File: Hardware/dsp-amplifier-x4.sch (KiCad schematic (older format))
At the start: 64 parts, among them J1 USBi, J2 EXT, J3 Raspberry_Pi_2_3, J4 Screw_Terminal_01x02, J5 Screw_Terminal_01x02, J6 Screw_Terminal_01x02, J7 Screw_Terminal_01x02, P1 Conn_WallPlug, Q1 STD2805, U1 ADAU1452

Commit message: new sockets
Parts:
- J4, J5, J6, J7, P1: footprint TerminalBlock:TerminalBlock_Wuerth_691311400102_P7.62mm -> terminal_connectors:wuerth_691216410002
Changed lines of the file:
@@
 F 0 "J4" H 14780 2792 50  0000 L CNN
 F 1 "Screw_Terminal_01x02" H 14780 2701 50  0000 L CNN
-F 2 "TerminalBlock:TerminalBlock_Wuerth_691311400102_P7.62mm" H 14700 2800 50  0001 C CNN
+F 2 "terminal_connectors:wuerth_691216410002" H 14700 2800 50  0001 C CNN
 F 3 "~" H 14700 2800 50  0001 C CNN
 	1    14700 2800
@@
 F 0 "J5" H 14780 3142 50  0000 L CNN
 F 1 "Screw_Terminal_01x02" H 14780 3051 50  0000 L CNN
-F 2 "TerminalBlock:TerminalBlock_Wuerth_691311400102_P7.62mm" H 14700 3150 50  0001 C CNN
+F 2 "terminal_connectors:wuerth_691216410002" H 14700 3150 50  0001 C CNN
 F 3 "~" H 14700 3150 50  0001 C CNN
 	1    14700 3150
@@
 F 0 "J6" H 14780 4492 50  0000 L CNN
 F 1 "Screw_Terminal_01x02" H 14780 4401 50  0000 L CNN
-F 2 "TerminalBlock:TerminalBlock_Wuerth_691311400102_P7.62mm" H 14700 4500 50  0001 C CNN
+F 2 "terminal_connectors:wuerth_691216410002" H 14700 4500 50  0001 C CNN
 F 3 "~" H 14700 4500 50  0001 C CNN
 	1    14700 4500
@@
 F 0 "J7" H 14780 4842 50  0000 L CNN
 F 1 "Screw_Terminal_01x02" H 14780 4751 50  0000 L CNN
-F 2 "TerminalBlock:TerminalBlock_Wuerth_691311400102_P7.62mm" H 14700 4850 50  0001 C CNN
+F 2 "terminal_connectors:wuerth_691216410002" H 14700 4850 50  0001 C CNN
 F 3 "~" H 14700 4850 50  0001 C CNN
 	1    14700 4850
@@
 F 0 "P1" H 9067 1375 50  0000 C CNN
 F 1 "Conn_WallPlug" H 9067 1284 50  0000 C CNN
-F 2 "TerminalBlock:TerminalBlock_Wuerth_691311400102_P7.62mm" H 9450 1050 50  0001 C CNN
+F 2 "terminal_connectors:wuerth_691216410002" H 9450 1050 50  0001 C CNN
 F 3 "~" H 9450 1050 50  0001 C CNN
 	1    9050 1050

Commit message: production v0.1 with gerber
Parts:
- added TP1: TestPoint, TestPoint:TestPoint_Pad_D1.0mm, symbol Connector:TestPoint
- added TP2: NCS, TestPoint:TestPoint_Pad_D1.0mm, symbol Connector:TestPoint
- added TP3: MISO, TestPoint:TestPoint_Pad_D1.0mm, symbol Connector:TestPoint
- added TP4: MOSI, TestPoint:TestPoint_Pad_D1.0mm, symbol Connector:TestPoint
- added TP5: SCLK, TestPoint:TestPoint_Pad_D1.0mm, symbol Connector:TestPoint
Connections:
- net +3.3VA: no longer Q1.3 (E), R4.1
- net +3V3: now also Q1.3 (E), R4.1
- net PI_MISO0: now also TP3.1
- net PI_MOSI0: now also TP4.1
- net PI_NCE0: now also TP2.1
- net PI_SCLK0: now also TP5.1
- net at U1.23 (CLKOUT): now also TP1.1
- no-connect marks 33 -> 35
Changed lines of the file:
@@
 F9 "CLK7" O R 10500 2450 60
 $EndSheet
-$Comp
-L DSP_AnalogDevices:ADAU1452 U1
-U 1 1 6065B65B
-P 3500 3650
-F 0 "U1" H 3500 5731 50  0000 C CNN
-F 1 "ADAU1452" H 3500 5640 50  0000 C CNN
-F 2 "Package_CSP:LFCSP-72-1EP_10x10mm_P0.5mm_EP5.3x5.3mm" H 3500 3650 50  0001 C CNN
-F 3 "https://www.analog.com/media/en/technical-documentation/data-sheets/ADAU1452_1451_1450.pdf" H 3500 3650 50  0001 C CNN
-	1    3500 3650
-	1    0    0    -1
-$EndComp
 Text Label 2000 2350 0    60   ~ 0
 DSP_CLOCK
@@
 Text Label 10850 7950 0    60   ~ 0
 PI_MISO0
-Wire Wire Line
-	10650 7950 11250 7950
-Wire Wire Line
-	11250 8050 10650 8050
 Text Label 10850 8150 0    60   ~ 0
 PI_SCLK0
-Wire Wire Line
-	11250 8150 10650 8150
 Text Label 8350 8350 0    60   ~ 0
 PI_MUTE
@@
 	1700 1450 2000 1450
 Connection ~ 2000 1450
-Text Label 4050 7050 2    60   ~ 0
-PVDD
 Text Label 3300 1250 3    60   ~ 0
 PVDD
@@
 Text Label 3700 9800 3    60   ~ 0
 AVDD
-NoConn ~ 4400 2350
 Text Label 4900 1950 2    60   ~ 0
 VDRIVE
@@
 	0    1    1    0
 $EndComp
-Wire Wire Line
-	4400 3350 4450 3350
 Wire Wire Line
 	4450 3450 4400 3450
@@
 Wire Wire Line
 	2000 4150 2600 4150
+Text Label 4050 7050 2    60   ~ 0
+IOVDD
+$Comp
+L Connector:TestPoint TP1
+U 1 1 6072217C
+P 4450 2350
+F 0 "TP1" V 4404 2538 50  0000 L CNN
+F 1 "TestPoint" V 4495 2538 50  0000 L CNN
+F 2 "TestPoint:TestPoint_Pad_D1.0mm" H 4650 2350 50  0001 C CNN
+F 3 "~" H 4650 2350 50  0001 C CNN
+	1    4450 2350
+	0    1    1    0
+$EndComp
+$Comp
+L DSP_AnalogDevices:ADAU1452 U1
+U 1 1 6065B65B
+P 3500 3650
+F 0 "U1" H 3500 5731 50  0000 C CNN
+F 1 "ADAU1452" H 3500 5640 50  0000 C CNN
+F 2 "Package_CSP:LFCSP-72-1EP_10x10mm_P0.5mm_EP5.3x5.3mm" H 3500 3650 50  0001 C CNN
+F 3 "https://www.analog.com/media/en/technical-documentation/data-sheets/ADAU1452_1451_1450.pdf" H 3500 3650 50  0001 C CNN
+	1    3500 3650
+	1    0    0    -1
+$EndComp
+Wire Wire Line
+	4450 2350 4400 2350
+NoConn ~ 4400 3350
+NoConn ~ 2600 4050
+NoConn ~ 2600 4250
+$Comp
+L Connector:TestPoint TP3
+U 1 1 607AA7B9
+P 11700 7950
+F 0 "TP3" V 11654 8138 50  0000 L CNN
+F 1 "MISO" V 11745 8138 50  0000 L CNN
+F 2 "TestPoint:TestPoint_Pad_D1.0mm" H 11900 7950 50  0001 C CNN
+F 3 "~" H 11900 7950 50  0001 C CNN
+	1    11700 7950
+	0    1    1    0
+$EndComp
+$Comp
+L Connector:TestPoint TP4
+U 1 1 607C870C
+P 12150 8050
+F 0 "TP4" V 12104 8238 50  0000 L CNN
+F 1 "MOSI" V 12195 8238 50  0000 L CNN
+F 2 "TestPoint:TestPoint_Pad_D1.0mm" H 12350 8050 50  0001 C CNN
+F 3 "~" H 12350 8050 50  0001 C CNN
+	1    12150 8050
+	0    1    1    0
+$EndComp
+$Comp
+L Connector:TestPoint TP5
+U 1 1 607E5FAD
+P 12600 8150
+F 0 "TP5" V 12554 8338 50  0000 L CNN
+F 1 "SCLK" V 12645 8338 50  0000 L CNN
+F 2 "TestPoint:TestPoint_Pad_D1.0mm" H 12800 8150 50  0001 C CNN
+F 3 "~" H 12800 8150 50  0001 C CNN
+	1    12600 8150
+	0    1    1    0
+$EndComp
+$Comp
+L Connector:TestPoint TP2
+U 1 1 6082322F
+P 11250 7850
+F 0 "TP2" V 11204 8038 50  0000 L CNN
+F 1 "NCS" V 11295 8038 50  0000 L CNN
+F 2 "TestPoint:TestPoint_Pad_D1.0mm" H 11450 7850 50  0001 C CNN
+F 3 "~" H 11450 7850 50  0001 C CNN
+	1    11250 7850
+	0    1    1    0
+$EndComp
+Wire Wire Line
+	10650 7950 11700 7950
+Wire Wire Line
+	10650 8050 12150 8050
+Wire Wire Line
+	10650 8150 12600 8150
 $EndSCHEMATC

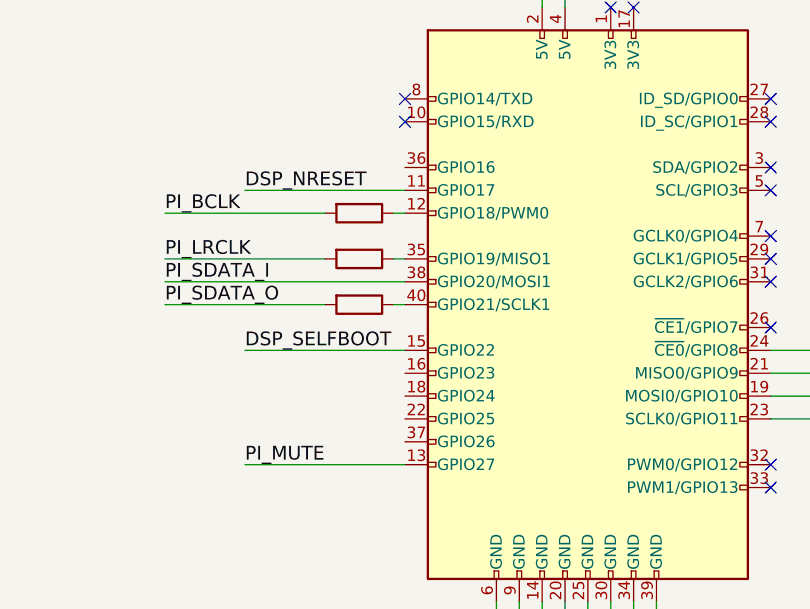
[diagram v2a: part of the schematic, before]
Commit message: fixed usbi/ext header positions
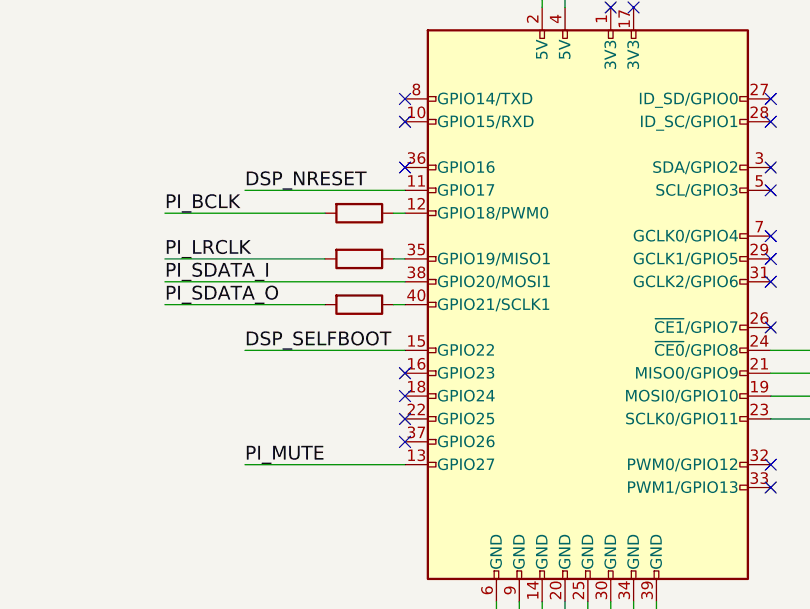
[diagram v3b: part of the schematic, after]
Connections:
- no-connect marks 35 -> 40
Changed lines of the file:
@@
 Wire Wire Line
 	10650 8150 12600 8150
+NoConn ~ 9050 7050
+NoConn ~ 9050 7950
+NoConn ~ 9050 8050
+NoConn ~ 9050 8150
+NoConn ~ 9050 8250
 $EndSCHEMATC

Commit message: hardware bugfixes
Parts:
- added U2: TSOP583xx, OptoDevice:Vishay_MINICAST-3Pin, symbol Interface_Optical:TSOP583xx
- RV1, RV2: footprint Potentiometer_THT:Potentiometer_Vishay_248GJ-249GJ_Single_Vertical -> Potentiometer_THT:Potentiometer_Bourns_PTV09A-1_Single_Vertical
- renumbered R20 to R15, R22 to R16, R23 to R17, R24 to R18, R25 to R19, R26 to R20, R27 to R21, R28 to R22, R29 to R23, R30 to R24
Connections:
- net +24V: no longer J2.1 (Pin_1)
- net +5VA: now also J2.1 (Pin_1)
- net GND: now also U2.2 (GND)
- net PI_3V3: now reaches J3.1 (3V3)
- net PI_3V3: now also U2.3 (Vs)
- net IR_INPUT: now reaches J3.3 (SDA/GPIO2)
- net IR_INPUT: now also U2.1 (OUT)
- no-connect marks 40 -> 38

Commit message: various bugfixes
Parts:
- removed TP1: TestPoint, TestPoint:TestPoint_Pad_D1.0mm, symbol Connector:TestPoint
- removed TP2: NCS, TestPoint:TestPoint_Pad_D1.0mm, symbol Connector:TestPoint
- removed TP3: MISO, TestPoint:TestPoint_Pad_D1.0mm, symbol Connector:TestPoint
- removed TP4: MOSI, TestPoint:TestPoint_Pad_D1.0mm, symbol Connector:TestPoint
- removed TP5: SCLK, TestPoint:TestPoint_Pad_D1.0mm, symbol Connector:TestPoint
- FB1: value 600/100M -> BLM18SP601SZ1D (600/100M)
- RV1, RV2: value R_POT -> PTV09A-1020F-B203
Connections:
- no-connect marks 38 -> 39
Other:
- moved on the sheet: RV1, RV2
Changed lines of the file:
@@
 Wire Wire Line
 	9650 6300 9650 6350
-Text Label 10850 7850 0    60   ~ 0
+Text Label 11250 7850 2    60   ~ 0
 PI_NCE0
 Wire Wire Line
 	11250 7850 10650 7850
-Text Label 10850 8050 0    60   ~ 0
+Text Label 11250 8050 2    60   ~ 0
 PI_MOSI0
-Text Label 10850 7950 0    60   ~ 0
+Text Label 11250 7950 2    60   ~ 0
 PI_MISO0
-Text Label 10850 8150 0    60   ~ 0
+Text Label 11250 8150 2    60   ~ 0
 PI_SCLK0
 Text Label 8350 8350 0    60   ~ 0
@@
 AR Path="/612BC3BD" Ref="FB1"  Part="1"
 F 0 "FB1" V 1326 6850 50  0000 C CNN
-F 1 "600/100M" V 1417 6850 50  0000 C CNN
+F 1 "BLM18SP601SZ1D (600/100M)" V 1417 6850 50  0000 C CNN
 F 2 "Inductor_SMD:L_0603_1608Metric_Pad1.05x0.95mm_HandSolder" V 1530 6850 50  0001 C CNN
 F 3 "~" H 1600 6850 50  0001 C CNN
@@
 L Device:R_POT RV1
 U 1 1 607C4CE2
-P 5850 2100
-F 0 "RV1" H 5781 2146 50  0000 R CNN
-F 1 "R_POT" H 5781 2055 50  0000 R CNN
-F 2 "Potentiometer_THT:Potentiometer_Bourns_PTV09A-1_Single_Vertical" H 5850 2100 50  0001 C CNN
-F 3 "~" H 5850 2100 50  0001 C CNN
-	1    5850 2100
+P 4950 1250
+F 0 "RV1" H 4881 1296 50  0000 R CNN
+F 1 "PTV09A-1020F-B203" H 4881 1205 50  0000 R CNN
+F 2 "Potentiometer_THT:Potentiometer_Bourns_PTV09A-1_Single_Vertical" H 4950 1250 50  0001 C CNN
+F 3 "~" H 4950 1250 50  0001 C CNN
+	1    4950 1250
 	1    0    0    -1
 $EndComp
@@
 L Device:R_POT RV2
 U 1 1 607C7CF2
-P 6850 2100
-F 0 "RV2" H 6781 2146 50  0000 R CNN
-F 1 "R_POT" H 6781 2055 50  0000 R CNN
-F 2 "Potentiometer_THT:Potentiometer_Bourns_PTV09A-1_Single_Vertical" H 6850 2100 50  0001 C CNN
-F 3 "~" H 6850 2100 50  0001 C CNN
-	1    6850 2100
-	1    0    0    -1
-$EndComp
-Text Label 5850 1650 3    60   ~ 0
-AVDD
-Wire Wire Line
-	5850 1650 5850 1900
-Wire Wire Line
-	5850 1900 6850 1900
-Wire Wire Line
-	6850 1900 6850 1950
-Connection ~ 5850 1900
-Wire Wire Line
-	5850 1900 5850 1950
-$Comp
-L power:GND #PWR021
-U 1 1 607F06EF
-P 5850 2300
-F 0 "#PWR021" H 5850 2050 50  0001 C CNN
-F 1 "GND" H 5850 2150 50  0000 C CNN
-F 2 "" H 5850 2300 50  0001 C CNN
-F 3 "" H 5850 2300 50  0001 C CNN
-	1    5850 2300
-	1    0    0    -1
-$EndComp
-Wire Wire Line
-	5850 2250 5850 2300
-$Comp
-L power:GND #PWR023
-U 1 1 608051CA
-P 6850 2300
-F 0 "#PWR023" H 6850 2050 50  0001 C CNN
-F 1 "GND" H 6850 2150 50  0000 C CNN
-F 2 "" H 6850 2300 50  0001 C CNN
-F 3 "" H 6850 2300 50  0001 C CNN
-	1    6850 2300
-	1    0    0    -1
-$EndComp
-Wire Wire Line
-	6850 2300 6850 2250
-Text Label 6350 2100 2    60   ~ 0
+P 5950 1250
+F 0 "RV2" H 5881 1296 50  0000 R CNN
+F 1 "PTV09A-1020F-B203" H 5881 1205 50  0000 R CNN
+F 2 "Potentiometer_THT:Potentiometer_Bourns_PTV09A-1_Single_Vertical" H 5950 1250 50  0001 C CNN
+F 3 "~" H 5950 1250 50  0001 C CNN
+	1    5950 1250
+	1    0    0    -1
+$EndComp
+Wire Wire Line
+	4950 800  4950 1050
+Wire Wire Line
+	4950 1050 5950 1050
+Wire Wire Line
+	5950 1050 5950 1100
+Connection ~ 4950 1050
+Wire Wire Line
+	4950 1050 4950 1100
+Text Label 5450 1250 2    60   ~ 0
 VPOT0
 Wire Wire Line
-	6000 2100 6350 2100
-Text Label 7350 2100 2    60   ~ 0
+	5100 1250 5450 1250
+Text Label 6450 1250 2    60   ~ 0
 VPOT1
 Wire Wire Line
-	7000 2100 7350 2100
+	6100 1250 6450 1250
 Text Label 2250 4750 0    60   ~ 0
 VPOT0
@@
 IOVDD
 $Comp
-L Connector:TestPoint TP1
-U 1 1 6072217C
-P 4450 2350
-F 0 "TP1" V 4404 2538 50  0000 L CNN
-F 1 "TestPoint" V 4495 2538 50  0000 L CNN
-F 2 "TestPoint:TestPoint_Pad_D1.0mm" H 4650 2350 50  0001 C CNN
-F 3 "~" H 4650 2350 50  0001 C CNN
-	1    4450 2350
-	0    1    1    0
-$EndComp
-$Comp
 L DSP_AnalogDevices:ADAU1452 U1
 U 1 1 6065B65B
@@
 	1    0    0    -1
 $EndComp
-Wire Wire Line
-	4450 2350 4400 2350
 NoConn ~ 4400 3350
 NoConn ~ 2600 4050
 NoConn ~ 2600 4250
-$Comp
-L Connector:TestPoint TP3
-U 1 1 607AA7B9
-P 11700 7950
-F 0 "TP3" V 11654 8138 50  0000 L CNN
-F 1 "MISO" V 11745 8138 50  0000 L CNN
-F 2 "TestPoint:TestPoint_Pad_D1.0mm" H 11900 7950 50  0001 C CNN
-F 3 "~" H 11900 7950 50  0001 C CNN
-	1    11700 7950
-	0    1    1    0
-$EndComp
-$Comp
-L Connector:TestPoint TP4
-U 1 1 607C870C
-P 12150 8050
-F 0 "TP4" V 12104 8238 50  0000 L CNN
-F 1 "MOSI" V 12195 8238 50  0000 L CNN
-F 2 "TestPoint:TestPoint_Pad_D1.0mm" H 12350 8050 50  0001 C CNN
-F 3 "~" H 12350 8050 50  0001 C CNN
-	1    12150 8050
-	0    1    1    0
-$EndComp
-$Comp
-L Connector:TestPoint TP5
-U 1 1 607E5FAD
-P 12600 8150
-F 0 "TP5" V 12554 8338 50  0000 L CNN
-F 1 "SCLK" V 12645 8338 50  0000 L CNN
-F 2 "TestPoint:TestPoint_Pad_D1.0mm" H 12800 8150 50  0001 C CNN
-F 3 "~" H 12800 8150 50  0001 C CNN
-	1    12600 8150
-	0    1    1    0
-$EndComp
-$Comp
-L Connector:TestPoint TP2
-U 1 1 6082322F
-P 11250 7850
-F 0 "TP2" V 11204 8038 50  0000 L CNN
-F 1 "NCS" V 11295 8038 50  0000 L CNN
-F 2 "TestPoint:TestPoint_Pad_D1.0mm" H 11450 7850 50  0001 C CNN
-F 3 "~" H 11450 7850 50  0001 C CNN
-	1    11250 7850
-	0    1    1    0
-$EndComp
-Wire Wire Line
-	10650 7950 11700 7950
-Wire Wire Line
-	10650 8050 12150 8050
-Wire Wire Line
-	10650 8150 12600 8150
 NoConn ~ 9050 7050
 NoConn ~ 9050 8050
 NoConn ~ 9050 8150
 NoConn ~ 9050 8250
-$Comp
-L power:+5VA #PWR024
-U 1 1 60933EE6
-P 8300 3000
-F 0 "#PWR024" H 8300 2850 50  0001 C CNN
-F 1 "+5VA" H 8315 3173 50  0000 C CNN
-F 2 "" H 8300 3000 50  0001 C CNN
-F 3 "" H 8300 3000 50  0001 C CNN
-	1    8300 3000
-	1    0    0    -1
-$EndComp
 $Comp
 L Interface_Optical:TSOP583xx U2
@@
 Wire Wire Line
 	12850 6900 12850 6950
-Text Label 11350 7050 2    60   ~ 0
+Text Label 11250 7050 2    60   ~ 0
 IR_INPUT
-Wire Wire Line
-	11350 7050 10650 7050
 Text Label 13250 6700 2    60   ~ 0
 IR_INPUT
@@
 Wire Wire Line
 	11100 5000 11750 5000
+Wire Wire Line
+	11250 7950 10650 7950
+Wire Wire Line
+	10650 8050 11250 8050
+Wire Wire Line
+	11250 8150 10650 8150
+Wire Wire Line
+	11250 7050 10650 7050
+NoConn ~ 4400 2350
+$Comp
+L power:+5VA #PWR0116
+U 1 1 609E250E
+P 8300 3000
+F 0 "#PWR0116" H 8300 2850 50  0001 C CNN
+F 1 "+5VA" H 8315 3173 50  0000 C CNN
+F 2 "" H 8300 3000 50  0001 C CNN
+F 3 "" H 8300 3000 50  0001 C CNN
+	1    8300 3000
+	1    0    0    -1
+$EndComp
+Wire Wire Line
+	5950 1450 5950 1400
+$Comp
+L power:GND #PWR023
+U 1 1 608051CA
+P 5950 1450
+F 0 "#PWR023" H 5950 1200 50  0001 C CNN
+F 1 "GND" H 5950 1300 50  0000 C CNN
+F 2 "" H 5950 1450 50  0001 C CNN
+F 3 "" H 5950 1450 50  0001 C CNN
+	1    5950 1450
+	1    0    0    -1
+$EndComp
+Wire Wire Line
+	4950 1400 4950 1450
+$Comp
+L power:GND #PWR021
+U 1 1 607F06EF
+P 4950 1450
+F 0 "#PWR021" H 4950 1200 50  0001 C CNN
+F 1 "GND" H 4950 1300 50  0000 C CNN
+F 2 "" H 4950 1450 50  0001 C CNN
+F 3 "" H 4950 1450 50  0001 C CNN
+	1    4950 1450
+	1    0    0    -1
+$EndComp
+Text Label 4950 800  3    60   ~ 0
+AVDD
 $EndSCHEMATC
